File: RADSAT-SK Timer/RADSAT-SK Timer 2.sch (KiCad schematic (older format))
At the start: 42 parts, among them J201 Conn_01x07, J202 Conn_01x05, J203 Conn_01x03, J204 Conn_01x02, J205 Conn_01x02, J206 Conn_01x02, J210 ZX62WRD-B-5PC, Q201 IRLML2060, Q202 IRLML2060, Q203 PJFET, Q204 PJFET, Q205 PJFET, Q206 PJFET, SW201 SW_Push, SW202 SW_Push, SW203 SW_Push, SW204 SW_Push, SW205 SW_Push, SW206 SW_Push, U202 LTC3440EMSPBF

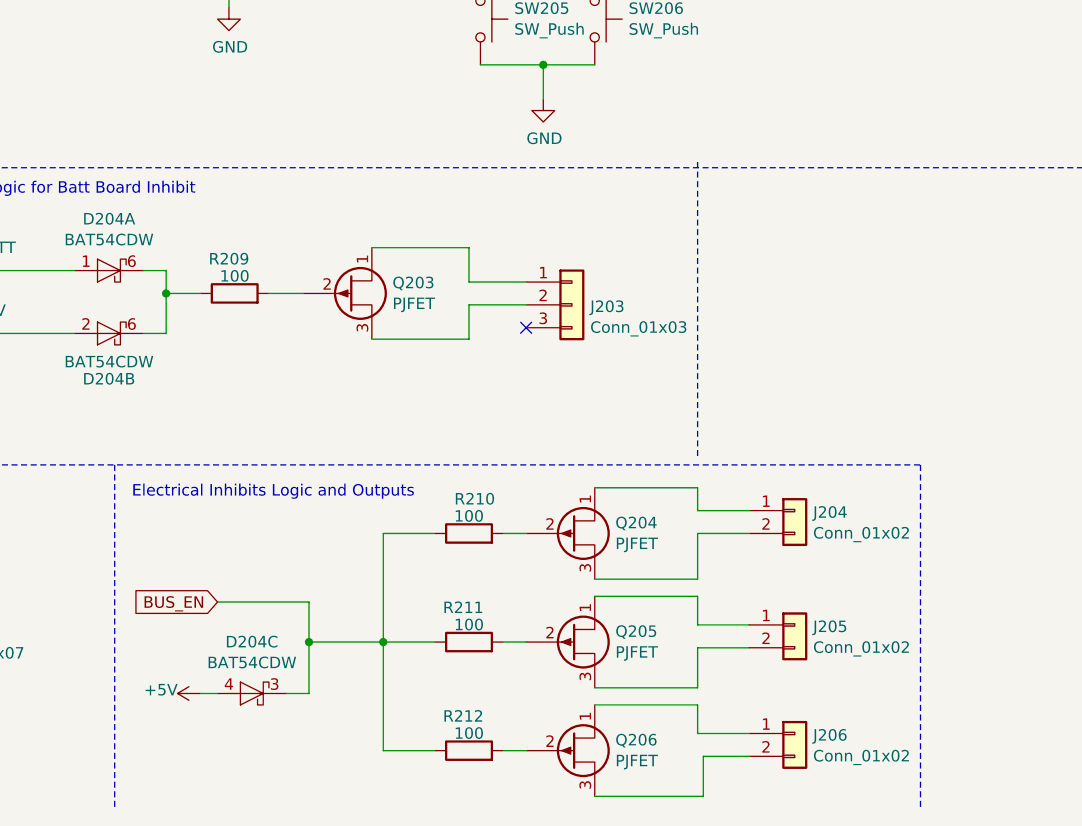
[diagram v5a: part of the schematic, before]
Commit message: use of a C117 solid state relay and another mosfet for isolated connection of the pins  ie we dont care about the pin characteristic now baby
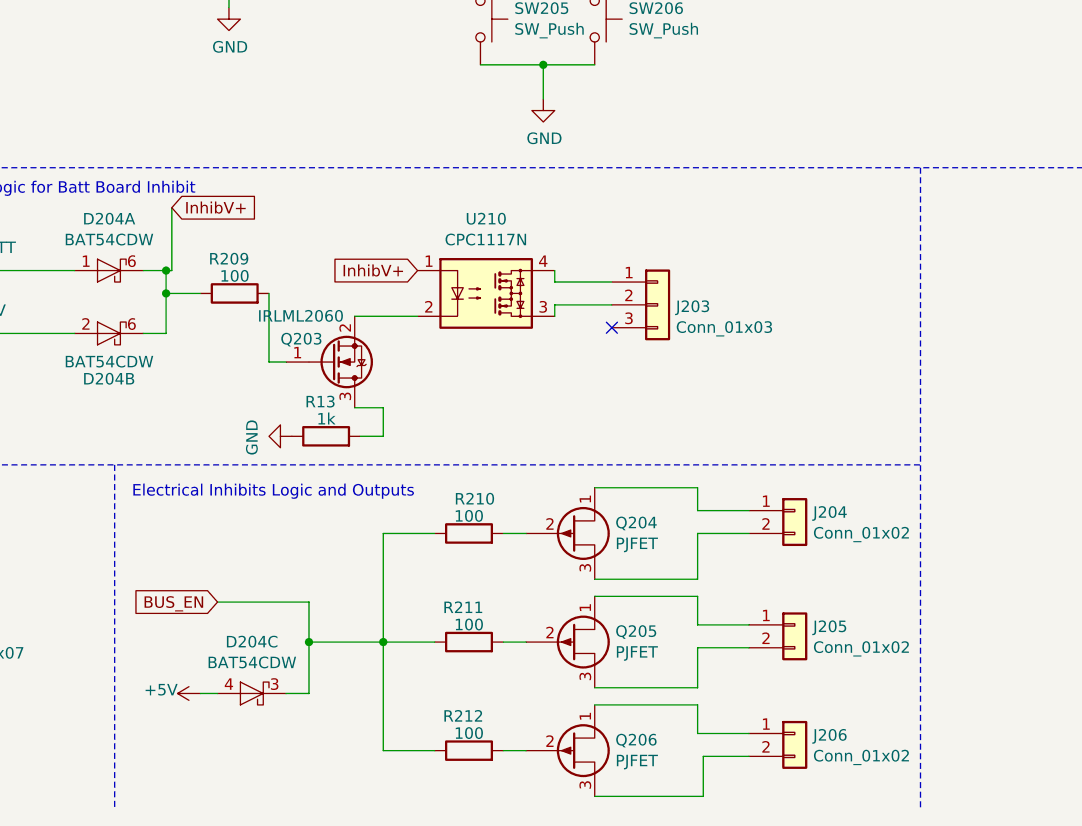
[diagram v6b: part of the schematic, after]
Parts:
- removed Q203: PJFET, Package_TO_SOT_THT:TO-92L_Inline_Wide, symbol Device:Q_PJFET_DGS
- added Q203: IRLML2060, Package_TO_SOT_SMD:SOT-23_Handsoldering, symbol Transistor_FET:IRLML2060
- added R13: 1k, Resistor_SMD:R_0805_2012Metric, symbol Device:R
- added U210: CPC1117N, Package_SO:SOP-4_3.8x4.1mm_P2.54mm, symbol Relay_SolidState:CPC1117N
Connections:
- net GND: now also R13.1
- net at J203.1 (Pin_1): now also U210.4
- net at J203.2 (Pin_2): now also U210.3
- net at R209.2: now also Q203.1 (G)
- net InhibV+: now reaches D204.6 (K), D204.6 (K), R209.1
- net InhibV+: now also U210.1
- new net: Q203.2 (S), U210.2
- new net: Q203.3 (D), R13.2
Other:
- moved on the sheet: J203
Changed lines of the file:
@@
 BUS_EN
-Wire Notes Line
-	6425 6300 6425 7800
 Wire Notes Line
 	475  6300 6425 6300
@@
 F 3 "~" H 5875 7000 50  0001 C CNN
 	1    5875 7000
-	1    0    0    -1
-$EndComp
-$Comp
-L Connector_Generic:Conn_01x03 J203
-U 1 1 615188F9
-P 4900 5600
-F 0 "J203" H 4980 5592 50  0000 L CNN
-F 1 "Conn_01x03" H 4980 5501 50  0000 L CNN
-F 2 "Connector_Hirose:Hirose_DF13-03P-1.25DSA_1x03_P1.25mm_Vertical" H 4900 5600 50  0001 C CNN
-F 3 "~" H 4900 5600 50  0001 C CNN
-	1    4900 5600
 	1    0    0    -1
 $EndComp
@@
 Text Notes 2175 5125 0    50   ~ 0
 RBF Logic for Batt Board Inhibit
-Wire Notes Line
-	5450 4975 5450 6275
 $Comp
 L CONN_ZX62WRD-B-5PC_HIR:ZX62WRD-B-5PC J210
@@
 Wire Wire Line
 	1300 5900 1300 6025
-NoConn ~ 4700 5700
 Connection ~ 6300 1850
 Wire Wire Line
 	6300 1850 7700 1850
-$Comp
-L Device:Q_PJFET_DGS Q203
-U 1 1 6167F061
-P 3925 5550
-F 0 "Q203" H 4115 5596 50  0000 L CNN
-F 1 "PJFET" H 4115 5505 50  0000 L CNN
-F 2 "Package_TO_SOT_THT:TO-92L_Inline_Wide" H 4125 5650 50  0001 C CNN
-F 3 "https://www.onsemi.com/pdf/datasheet/j175-d.pdf" H 3925 5550 50  0001 C CNN
-	1    3925 5550
-	1    0    0    -1
-$EndComp
 Wire Wire Line
 	3125 5450 3125 5550
@@
 Wire Wire Line
 	5450 7275 5000 7275
-Wire Wire Line
-	4025 5350 4450 5350
-Wire Wire Line
-	4450 5350 4450 5500
-Wire Wire Line
-	4450 5500 4700 5500
-Wire Wire Line
-	4700 5600 4450 5600
-Wire Wire Line
-	4450 5600 4450 5750
-Wire Wire Line
-	4450 5750 4025 5750
 Wire Wire Line
 	3025 5725 3125 5725
@@
 Wire Wire Line
 	4600 7550 4700 7550
-Wire Wire Line
-	3575 5550 3725 5550
 $Comp
 L Device:D_Schottky D203
@@
 	-1   0    0    1
 $EndComp
+$Comp
+L Transistor_FET:IRLML2060 Q?
+U 1 1 61760C64
+P 3850 5850
+AR Path="/61760C64" Ref="Q?"  Part="1"
+AR Path="/602E25D3/61760C64" Ref="Q203"  Part="1"
+F 0 "Q203" H 3625 5750 50  0000 L CNN
+F 1 "IRLML2060" H 3525 5650 50  0000 L CNN
+F 2 "Package_TO_SOT_SMD:SOT-23_Handsoldering" H 4050 5775 50  0001 L CIN
+F 3 "https://www.infineon.com/dgdl/irlml2060pbf.pdf?fileId=5546d462533600a401535664b7fb25ee" H 3850 5850 50  0001 L CNN
+	1    3850 5850
+	1    0    0    1
+$EndComp
+Text GLabel 3150 5175 2    50   Input ~ 0
+InhibV+
+Wire Wire Line
+	3150 5175 3150 5450
+Wire Wire Line
+	3150 5450 3125 5450
+Connection ~ 3125 5450
+$Comp
+L power:GND #PWR0118
+U 1 1 6177DA1C
+P 3675 6175
+F 0 "#PWR0118" H 3675 5925 50  0001 C CNN
+F 1 "GND" H 3680 6002 50  0000 C CNN
+F 2 "" H 3675 6175 50  0001 C CNN
+F 3 "" H 3675 6175 50  0001 C CNN
+	1    3675 6175
+	0    1    1    0
+$EndComp
+Wire Notes Line
+	6425 5000 6425 7800
+Wire Wire Line
+	4825 5500 4825 5450
+Wire Wire Line
+	4825 5600 4825 5650
+Wire Wire Line
+	3575 5550 3575 5850
+Wire Wire Line
+	3575 5850 3650 5850
+Text GLabel 4225 5450 0    50   Input ~ 0
+InhibV+
+$Comp
+L Device:R R13
+U 1 1 617F0E83
+P 3825 6175
+F 0 "R13" V 3975 6200 50  0000 C CNN
+F 1 "1k" V 3900 6175 50  0000 C CNN
+F 2 "Resistor_SMD:R_0805_2012Metric" V 3755 6175 50  0001 C CNN
+F 3 "~" H 3825 6175 50  0001 C CNN
+	1    3825 6175
+	0    -1   -1   0
+$EndComp
+Wire Wire Line
+	3950 6050 4075 6050
+Wire Wire Line
+	4075 6050 4075 6175
+Wire Wire Line
+	4075 6175 3975 6175
+$Comp
+L Connector_Generic:Conn_01x03 J203
+U 1 1 615188F9
+P 5275 5600
+F 0 "J203" H 5355 5592 50  0000 L CNN
+F 1 "Conn_01x03" H 5355 5501 50  0000 L CNN
+F 2 "Connector_Hirose:Hirose_DF13-03P-1.25DSA_1x03_P1.25mm_Vertical" H 5275 5600 50  0001 C CNN
+F 3 "~" H 5275 5600 50  0001 C CNN
+	1    5275 5600
+	1    0    0    -1
+$EndComp
+NoConn ~ 5075 5700
+Wire Wire Line
+	5075 5500 4825 5500
+Wire Wire Line
+	5075 5600 4825 5600
+$Comp
+L Relay_SolidState:CPC1117N U210
+U 1 1 61804531
+P 4525 5550
+F 0 "U210" H 4525 5875 50  0000 C CNN
+F 1 "CPC1117N" H 4525 5784 50  0000 C CNN
+F 2 "Package_SO:SOP-4_3.8x4.1mm_P2.54mm" H 4325 5350 50  0001 L CIN
+F 3 "http://www.ixysic.com/home/pdfs.nsf/www/CPC1117N.pdf/$file/CPC1117N.pdf" H 4475 5550 50  0001 L CNN
+	1    4525 5550
+	1    0    0    -1
+$EndComp
+Wire Wire Line
+	3950 5650 4225 5650
 $EndSCHEMATC

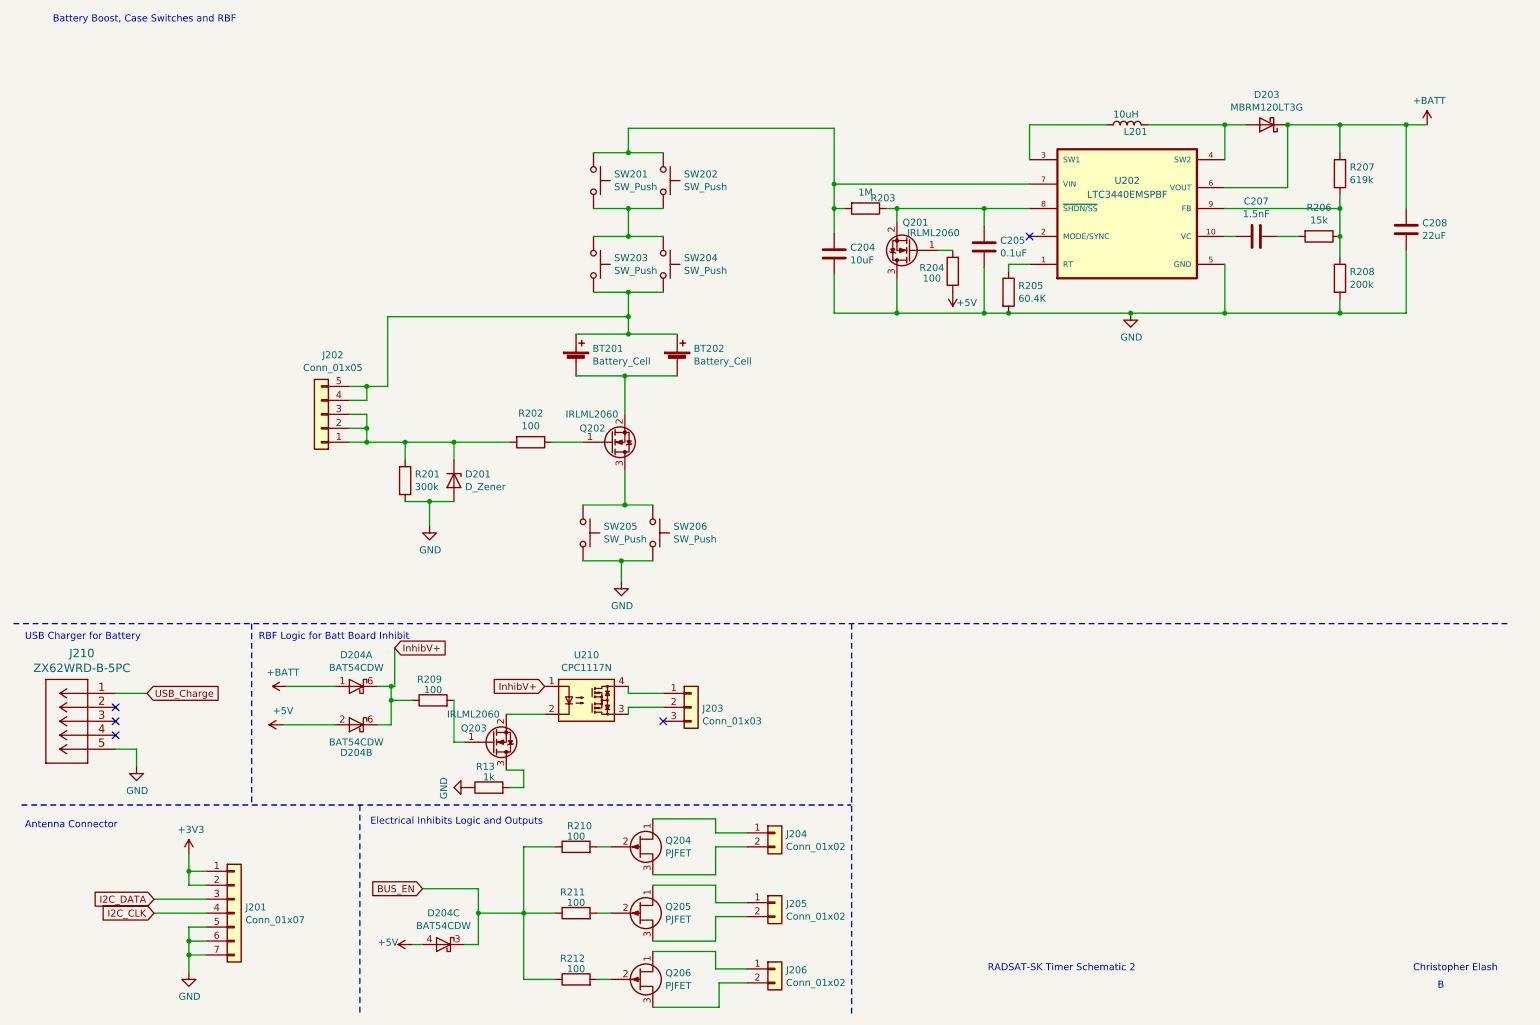
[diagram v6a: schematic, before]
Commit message: actually did the other relays for the inhibits, played around with layout stuff
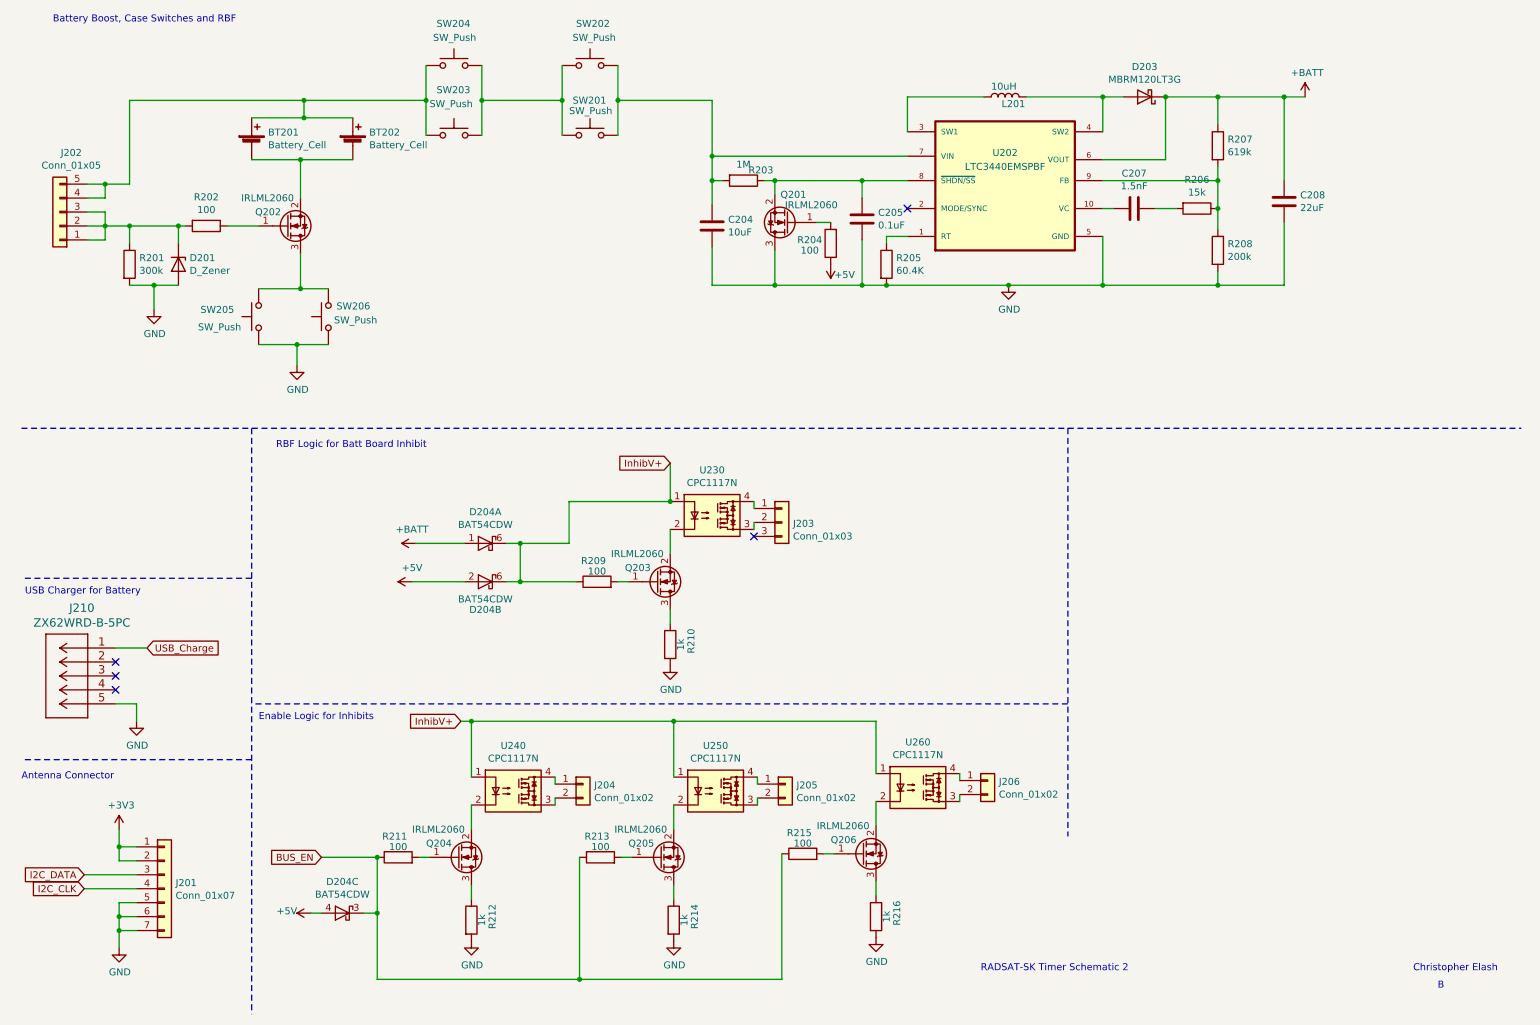
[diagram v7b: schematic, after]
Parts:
- removed Q204, Q205, Q206: PJFET, Package_TO_SOT_THT:TO-92L_Inline_Wide, symbol Device:Q_PJFET_DGS
- removed R210: 100, Resistor_SMD:R_0805_2012Metric, symbol Device:R
- added Q204, Q205, Q206: IRLML2060, Package_TO_SOT_SMD:SOT-23_Handsoldering, symbol Transistor_FET:IRLML2060
- added R213, R215: 100, Resistor_SMD:R_0805_2012Metric, symbol Device:R
- added R214, R216: 1k, Resistor_SMD:R_0805_2012Metric, symbol Device:R
- added U240, U250, U260: CPC1117N, Package_SO:SOP-4_3.8x4.1mm_P2.54mm, symbol Relay_SolidState:CPC1117N
- R212: value 100 -> 1k
- renumbered R13 to R210, U210 to U230
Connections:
- net BUS_EN: now also R213.1, R215.1; no longer R212.1
- net GND: now also R210.2, R212.2, SW205.1, SW206.1, R214.2, R216.2; no longer R210.1, SW205.2, SW206.2
- net InhibV+: now also U240.1, U250.1, U260.1
- net at BT201.1 (+), BT202.1 (+), J202.4 (Pin_4)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: now also SW203.1, SW204.1; no longer SW203.2, SW204.2
- net at C204.1, R203.2, U202.7 (VIN): now also SW201.2, SW202.2; no longer SW201.1, SW202.1
- net at J204.1 (Pin_1): now also U240.4
- net at J204.2 (Pin_2): now also U240.3
- net at J206.1 (Pin_1): now also U260.4
- net at J206.2 (Pin_2): now also U260.3
- net at J205.1 (Pin_1): now also U250.4
- net at J205.2 (Pin_2): now also U250.3
- net at R211.2: now also Q204.1 (G)
- net at Q203.3 (D): now also R210.1; no longer R210.2
- new net: Q202.3 (D), SW205.2, SW206.2
- new net: SW201.1, SW202.1, SW203.2, SW204.2
- new net: Q205.1 (G), R213.2
- new net: Q205.2 (S), U250.2
- new net: Q205.3 (D), R214.1
- new net: Q206.1 (G), R215.2
- new net: Q206.2 (S), U260.2
- new net: Q206.3 (D), R216.1
- new net: Q204.2 (S), U240.2
- new net: Q204.3 (D), R212.1
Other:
- note added: "Enable Logic for Inhibits"
- note removed: "Electrical Inhibits Logic and Outputs"
- moved on the sheet: BT201, BT202, C204, C205, C207, C208, D201, D203, D204A, D204B, D204C, J201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
